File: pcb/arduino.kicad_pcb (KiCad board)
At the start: 2 copper layers, 84 parts, among them J1 Conn_Coaxial_Power, SW1 SW_SPDT, U1 ATMEGA328-PU, U2 L7805, Y1 16MHz

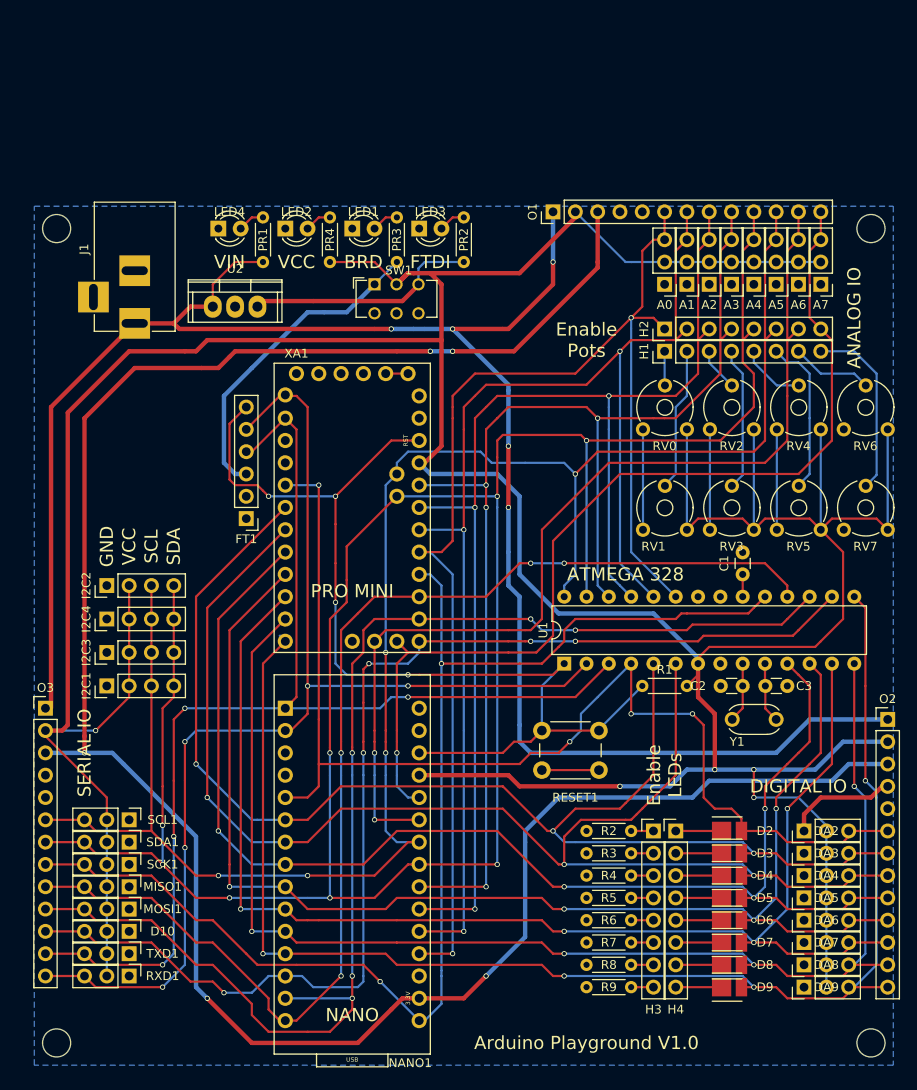
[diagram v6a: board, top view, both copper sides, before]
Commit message: Replaced surface mount LEDs with rectangular through hole. Removed PRO-Mini FTDI Header pins from the footprint.
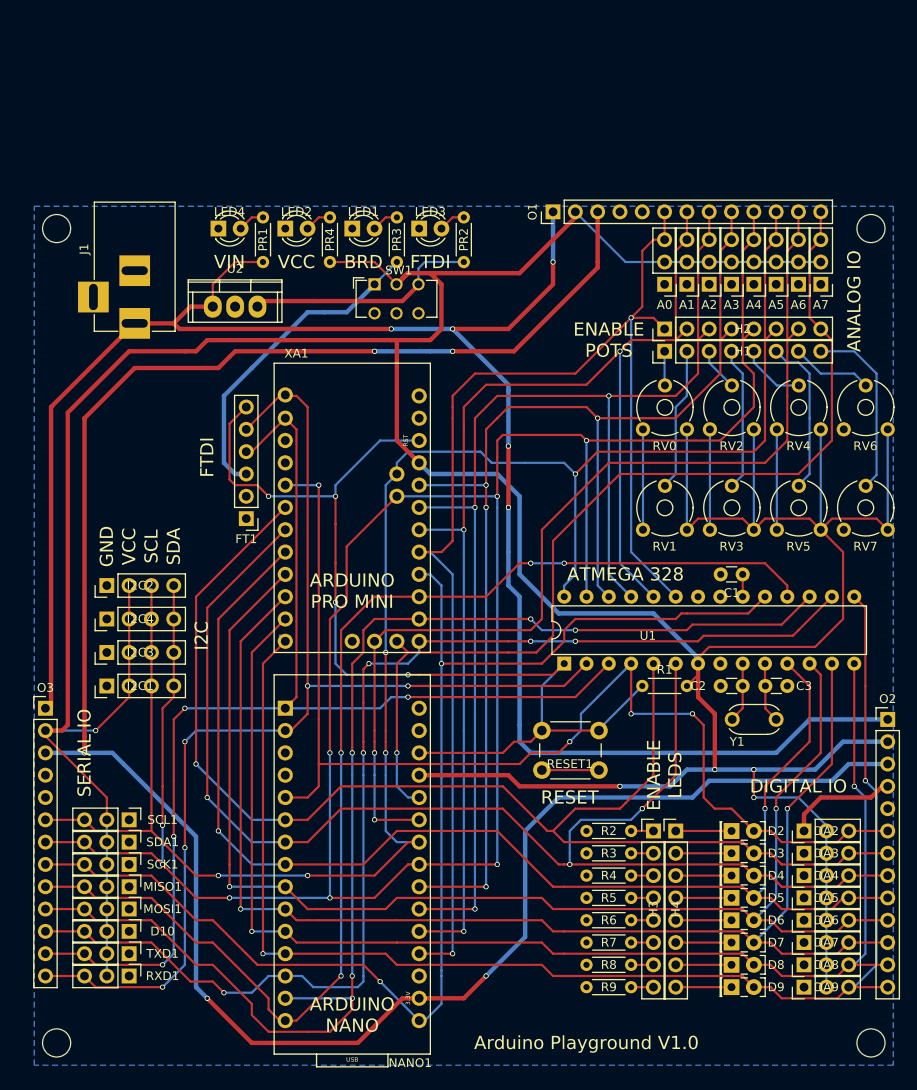
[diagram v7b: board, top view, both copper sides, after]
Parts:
- D2, D3, D4, D5, D6, D7, D8, D9: footprint LEDs:LED_PLCC_2835 -> LEDs:LED_Rectangular_W5.0mm_H2.0mm
- XA1: footprint Arduino:Arduino_ProMini -> Arduino:Arduino_ProMini_NoFTDI
- turned C1 to 180 degrees
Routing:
- net /D4: track 153.4 -> 150.7 mm, vias 3 -> 4
- net Net-(XA1-PadGND3): track 2.54 -> 0.00 mm
- net /D9: track 161.2 -> 158.8 mm, vias 4 -> 3
- net /D5: track 151.9 -> 149.5 mm, vias 4 -> 3
- net /D6: track 151.5 -> 149.7 mm, vias 4 -> 3
- net /D8: track 149.9 -> 148.1 mm, vias 4 -> 3
- net /D7: track 151.2 -> 149.4 mm, vias 4 -> 3
- net /D2: track 131.6 -> 130.2 mm
- net /D3: track 149.8 -> 148.6 mm, vias 3 -> 2
- net Net-(D9-Pad1): track 5.22 -> 6.35 mm
- net Net-(D8-Pad1): track 5.22 -> 6.35 mm
- net Net-(D7-Pad1): track 5.22 -> 6.35 mm
- net Net-(D6-Pad1): track 5.22 -> 6.35 mm
- net Net-(D5-Pad1): track 5.22 -> 6.35 mm
- net Net-(D4-Pad1): track 5.22 -> 6.35 mm
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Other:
- board text added: "ARDUINO NANO"
- board text added: "ARDUINO PRO MINI"
- board text added: "ENABLE LEDS"
- board text added: "ENABLE POTS"
- board text added: "I2C"
- board text added: "RESET"
- board text removed: "Enable LEDs"
- board text removed: "Enable Pots"
- board text removed: "NANO"
- board text removed: "PRO MINI"

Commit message: Fix board size, and moved I2C headers.
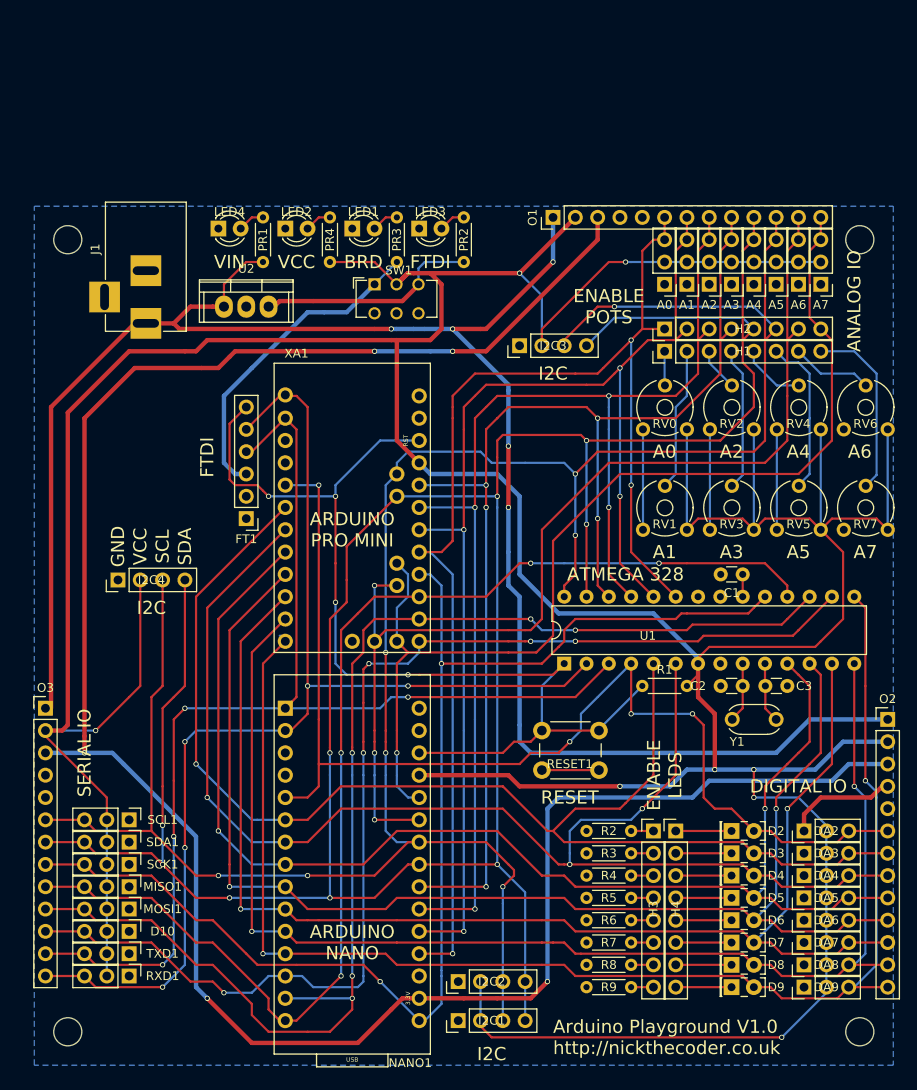
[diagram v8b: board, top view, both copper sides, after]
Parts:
- moved I2C2 60.3 mm to (111.1, 120.0)
- moved I2C3 58.5 mm to (118.1, 47.6)
- moved I2C1 55.2 mm to (111.1, 124.5)
- moved I2C4 4.62 mm to (72.4, 74.3)
- moved ? 1.80 mm to (156.8, 35.6)
- moved ? 1.80 mm to (156.8, 125.7)
- moved ? 1.80 mm to (66.7, 35.6)
- moved ? 1.80 mm to (66.7, 125.7)
- moved U2 1.27 mm to (87.0, 43.2)
- moved J1 1.27 mm to (75.6, 45.1)
- moved O1 0.64 mm to (121.9, 33.0)
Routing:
- net /VCC: track 476.2 -> 541.5 mm, vias 5 -> 8
- net /A5: track 208.7 -> 267.1 mm, vias 5 -> 8
- net /A4: track 270.0 -> 311.2 mm, vias 8 -> 9
- net /A7: track 112.8 -> 122.8 mm
- net /A6: track 116.2 -> 125.1 mm, vias 2 -> 3
- net /A0: track 149.3 -> 146.4 mm, vias 2 -> 3
- net /3V3: track 249.8 -> 252.4 mm
- net Net-(PR2-Pad2): track 27.6 -> 25.4 mm
- net /A1: track 143.6 -> 141.7 mm, vias 3 -> 4
- net /VIN: track 214.7 -> 213.2 mm
- net /A3: vias 4 -> 5
- net /A2: vias 3 -> 4
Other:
- board text added: "A0"
- board text added: "A1"
- board text added: "A2"
- board text added: "A3"
- board text added: "A4"
- board text added: "A5"
- board text added: "A6"
- board text added: "A7"
- board text added: "Arduino Playground V1.0 http://nickthecoder.co.uk"
- board text removed: "Arduino Playground V1.0"
